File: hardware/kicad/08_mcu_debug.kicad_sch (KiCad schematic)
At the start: 30 parts, among them J801 SWD, J802 UART (bench), SW801 RESET, U801 STM32G474VET6, U802 MAX6369 (candidate), Y801 8MHz

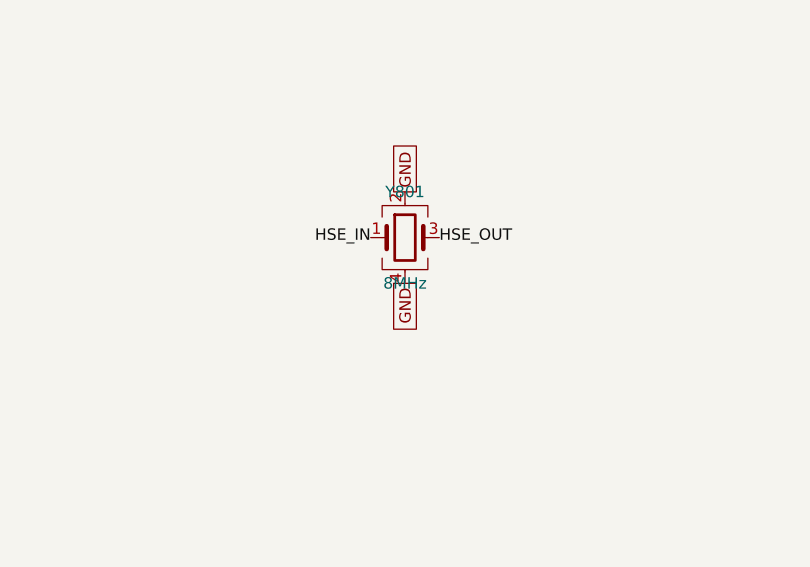
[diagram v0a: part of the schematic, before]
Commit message: sem-motor-controller: CAN/CHUDS integration specifics, rules reconciliation, input sheet
- CHUDS evidence (urban-concept@c422c0f): CAN FD 500k/2M at 80%/80%,
  classic frames dropped as ForeignFrame, 0x300-0x7FF reserved for future
  classes, accept-all MCP filters, Emergency STOP semantics; no wiring docs.
- FDCAN must run in FD mode with matching data-phase timing: bit-timing
  calculator shows 8 MHz cannot reach the 80% data sample point -> crystal
  changed to 40 MHz in the schematic draft; platform requirements updated.
- VCU-side raw SocketCAN bridge proposal (classic semmc frames on the FD
  bus) with unit tests (no AF_CAN in this container: socket path untested).
- Rules reconciliation per hardware/software element; ADR-0009 scope
  clarified (no blanket vendor-SDK ruling); organiser questions.
- Attachments bk4000tg_kicad.zip / telemetry.pdf: not found (uploads,
  attach, filesystem, Drive) - recorded.
- One-page vehicle-team input sheet; open parameters updated.

Co-Authored-By: Claude Opus 5.5 <noreply@anthropic.com>
Claude-Session: https://claude.ai/code/session_01GHmHZxA3w1n62SULRNT3dB
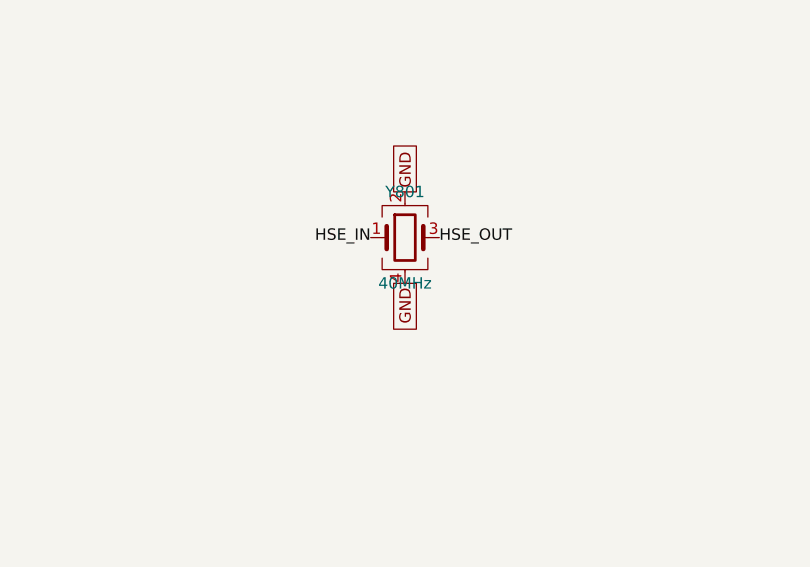
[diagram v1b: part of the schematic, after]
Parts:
- Y801: value 8MHz -> 40MHz; Rating_basis FDCAN kernel clock (500 kbit/s = 16 tq); tolerance per CAN 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 -> FDCAN kernel clock: 500k/2M CAN FD at 80 %/80 % needs 20 or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
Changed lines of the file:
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@@
       (effects (font (size 1.27 1.27)))
     )
-    (property "Value" "8MHz" (id 1) (at 264.16 238.76000000000002 0)
+    (property "Value" "40MHz" (id 1) (at 264.16 238.76000000000002 0)
       (effects (font (size 1.27 1.27)))
     )
@@
       (effects (font (size 1.27 1.27)) hide)
     )
-    (property "Rating_basis" "FDCAN kernel clock (500 kbit/s = 16 tq); tolerance per CAN oscillator budget" (id 5) (at 264.16 233.68 0)
+    (property "Rating_basis" "FDCAN kernel clock: 500k/2M CAN FD at 80 %/80 % needs 20 or 40 MHz (docs/generated/can_bit_timing.md); 8 MHz cannot place the data-phase SP" (id 5) (at 264.16 233.68 0)
       (effects (font (size 1.27 1.27)) hide)
     )

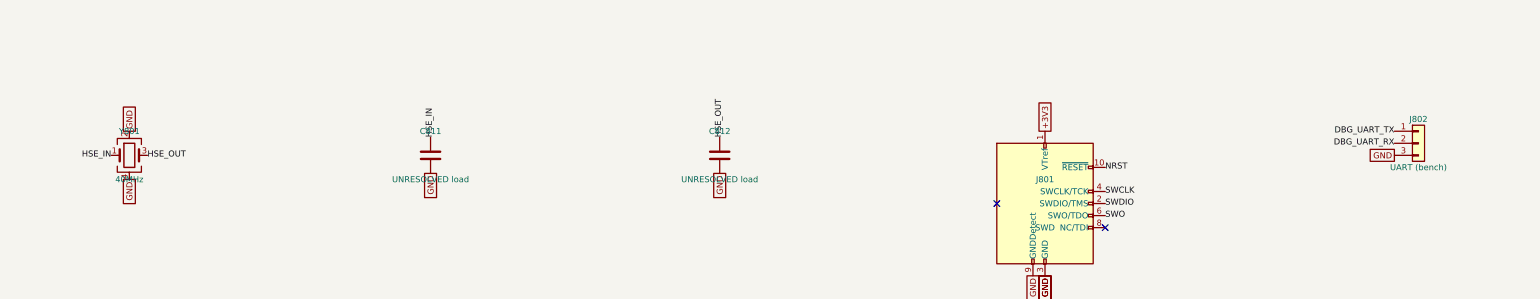
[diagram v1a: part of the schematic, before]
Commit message: sem-motor-controller v0.3: vehicle-interface provenance, transport-neutral core, clock trees, schematic checks
Provenance: the Cornell repositories are reference projects. Every place
that treated CHUDS / CAN FD / its VCU / 40 MHz as our vehicle is relabelled
or corrected (docs/PROVENANCE_AUDIT.md); the v0.2 checkpoint is preserved
with an errata banner.

Firmware: the core is transport-neutral (mc_core_on_msg_rx /
mc_core_msg_tx_poll / mc_core_on_link_state). CAN is one binding
(src/transport/mc_can_binding.c) whose 64-identifier block base is the new
calibration parameter supervision.can_id_base (id 164, rule 40, null in the
unconfigured config). ADR-0012. Tests: block relocation with a full ECO
engagement at 0x500, neutral API, rule-40 C/Python parity.

Clocking: tools/clock_tree.py evaluates 28 complete clock trees x 4 bus
cases from ST register widths and HAL ranges; the v0.2 "40 MHz required"
claim is withdrawn and the crystal is unselected until the bus is known.

Schematic: INA228 pins renumbered (KiCad-library cross-check, secondary);
DRV8353S stays an explicit placeholder; crystal unselected; PWR_FLAGs added
after a new pin-type check (not an ERC) found 6 undriven-rail errors.
Real KiCad ERC not run (KiCad 7 has no CLI ERC; tools/run_kicad_erc.sh).

Telematics: combined architecture with the STM32U575 / CAN 2.0B / LTE-MQTT
proposal (supervisor and CSIA placement, torque-request and driver-
authorization paths, pit/cloud outside the control chain), interface
difference table, generated DBC, logging-capacity and auxiliary-power
budget. Validation language separates command ceilings, envelope ramp,
phase current and battery current. CSIA: component attribution and a
next-evaluation plan; frozen results unchanged, nothing re-run.

Verified on the host: ctest 6/6 (4,006 checks), pytest 199 passed,
ARM core build 0 warnings, generators current, KiCad connectivity 0
problems. Nothing on hardware.

Co-Authored-By: Claude Opus 5.5 <noreply@anthropic.com>
Claude-Ses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
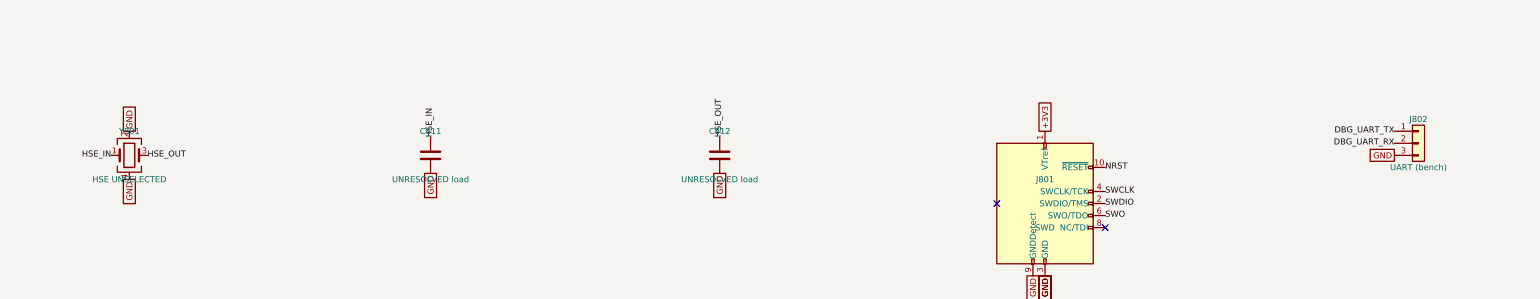
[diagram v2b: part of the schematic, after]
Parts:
- Y801: value 40MHz -> HSE UNSELECTED; Rating_basis FDCAN kernel clock: 500k/2M CAN FD at 80 %/80 % needs 20 or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 -> frequency NOT selected: depends on the vehicle bus (classic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; Status CANDIDATE -> UNRESOLVED
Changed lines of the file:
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@@
       (effects (font (size 1.27 1.27)))
     )
-    (property "Value" "40MHz" (id 1) (at 264.16 238.76000000000002 0)
+    (property "Value" "HSE UNSELECTED" (id 1) (at 264.16 238.76000000000002 0)
       (effects (font (size 1.27 1.27)))
     )
@@
       (effects (font (size 1.27 1.27)) hide)
     )
-    (property "Status" "CANDIDATE" (id 4) (at 264.16 233.68 0)
+    (property "Status" "UNRESOLVED" (id 4) (at 264.16 233.68 0)
       (effects (font (size 1.27 1.27)) hide)
     )
-    (property "Rating_basis" "FDCAN kernel clock: 500k/2M CAN FD at 80 %/80 % needs 20 or 40 MHz (docs/generated/can_bit_timing.md); 8 MHz cannot place the data-phase SP" (id 5) (at 264.16 233.68 0)
+    (property "Rating_basis" "frequency NOT selected: depends on the vehicle bus (classic or FD, bit rates) and the CPU frequency; candidates 8-40 MHz in hardware/timing/clock_tree_alternatives.md. The v0.2 '40 MHz required' claim is withdrawn." (id 5) (at 264.16 233.68 0)
       (effects (font (size 1.27 1.27)) hide)
     )
@@
     (pin "9")
   )
-  (symbol (lib_id "Connector_Generic:Conn_01x03") (at 535.94 231.14000000000001 0) (unit 1)
+  (symbol (lib_id "Connector_Generic:Conn_01x03") (at 535.94 231.14 0) (unit 1)
     (in_bom yes) (on_board yes)
-    (property "Reference" "J802" (id 0) (at 535.94 226.06 0)
+    (property "Reference" "J802" (id 0) (at 535.94 226.05999999999997 0)
       (effects (font (size 1.27 1.27)))
     )
-    (property "Value" "UART (bench)" (id 1) (at 535.94 236.22000000000003 0)
+    (property "Value" "UART (bench)" (id 1) (at 535.94 236.22 0)
       (effects (font (size 1.27 1.27)))
     )
-    (property "Footprint" "" (id 2) (at 535.94 231.14000000000001 0)
+    (property "Footprint" "" (id 2) (at 535.94 231.14 0)
       (effects (font (size 1.27 1.27)) hide)
     )
-    (property "Datasheet" "" (id 3) (at 535.94 231.14000000000001 0)
+    (property "Datasheet" "" (id 3) (at 535.94 231.14 0)
       (effects (font (size 1.27 1.27)) hide)
     )
-    (property "Status" "bench only; not populated for competition" (id 4) (at 535.94 231.14000000000001 0)
+    (property "Status" "bench only; not populated for competition" (id 4) (at 535.94 231.14 0)
       (effects (font (size 1.27 1.27)) hide)
     )
